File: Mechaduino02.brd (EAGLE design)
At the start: 41.9 x 41.9 mm, 64 parts, among them IC1 SAMD21G18A-AUT, Q1 BSS138, Q2 NFET, Q3 BSS138, Q4 BSS138, Q5 BSS138, U1 TLV70233PDBVR, Y1 32,768Khz

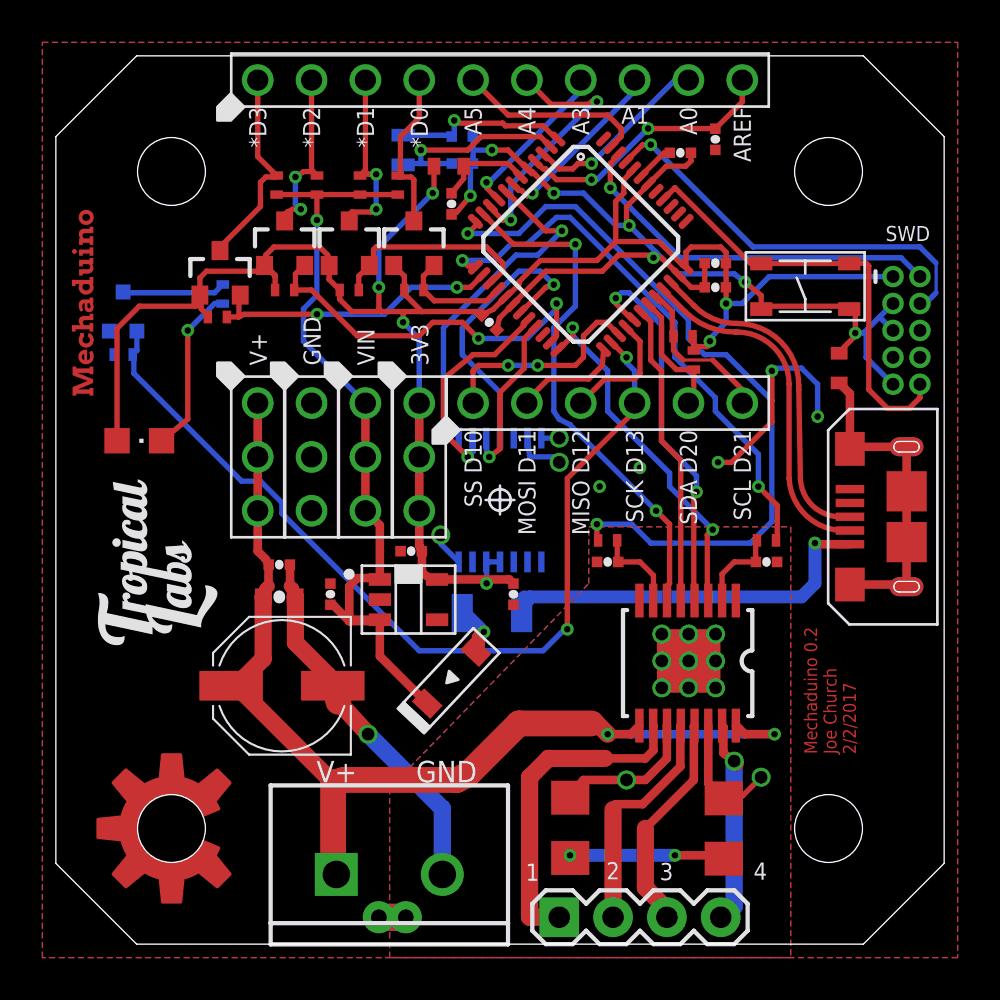
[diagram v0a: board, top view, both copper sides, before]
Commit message: via stitching
cleaned up ground pours
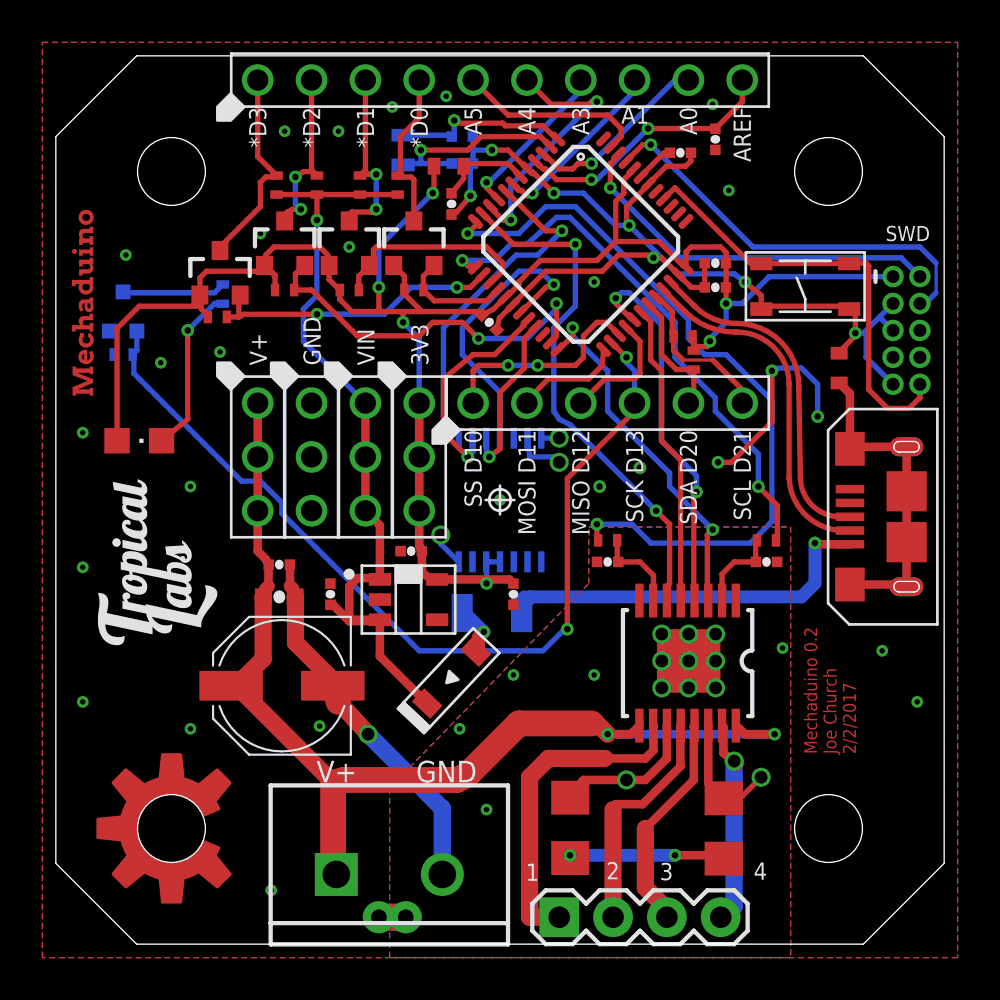
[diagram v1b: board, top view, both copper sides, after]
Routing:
- net GND2: vias 12 -> 17
- net GND: vias 12 -> 34
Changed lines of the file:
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@@
 <wire x1="0" y1="38.1" x2="3.81" y2="41.91" width="0" layer="20"/>
 <wire x1="0" y1="3.81" x2="0" y2="38.1" width="0" layer="20"/>
+<polygon width="0.4064" layer="41">
+<vertex x="-2.159" y="35.306"/>
+<vertex x="1.778" y="35.306"/>
+<vertex x="1.778" y="34.544"/>
+<vertex x="1.651" y="34.544"/>
+<vertex x="1.651" y="25.908"/>
+<vertex x="-1.651" y="25.908"/>
+<vertex x="-1.524" y="25.527"/>
+<vertex x="-2.159" y="25.527"/>
+</polygon>
+<polygon width="0.4064" layer="41">
+<vertex x="37.211" y="33.782"/>
+<vertex x="34.925" y="33.782"/>
+<vertex x="34.925" y="32.893"/>
+<vertex x="38.735" y="32.893"/>
+<vertex x="38.735" y="32.639"/>
+<vertex x="40.386" y="32.639"/>
+<vertex x="40.132" y="32.639"/>
+<vertex x="40.132" y="34.036"/>
+<vertex x="37.211" y="34.036"/>
+</polygon>
+<wire x1="10.541" y1="15.748" x2="10.541" y2="13.208" width="0.4064" layer="41"/>
+<wire x1="10.541" y1="13.208" x2="11.049" y2="13.208" width="0.4064" layer="41"/>
 </plain>
 <attributes>
@@
 <via x="27.559" y="22.479" extent="1-16" drill="0.3048"/>
 <via x="25.654" y="21.59" extent="1-16" drill="0.3048"/>
+<via x="10.795" y="38.354" extent="1-16" drill="0.254" diameter="0.254"/>
+<via x="13.335" y="38.354" extent="1-16" drill="0.254" diameter="0.254"/>
+<via x="13.843" y="32.893" extent="1-16" drill="0.254" diameter="0.254"/>
+<via x="15.875" y="39.497" extent="1-16" drill="0.254" diameter="0.254"/>
+<via x="3.302" y="32.512" extent="1-16" drill="0.254" diameter="0.254"/>
+<via x="20.955" y="20.955" extent="1-16" drill="0.254" diameter="0.254"/>
+<via x="6.35" y="21.59" extent="1-16" drill="0.254" diameter="0.254"/>
+<via x="1.27" y="24.13" extent="1-16" drill="0.254" diameter="0.254"/>
+<via x="1.27" y="11.43" extent="1-16" drill="0.254" diameter="0.254"/>
+<via x="6.35" y="10.16" extent="1-16" drill="0.254" diameter="0.254"/>
+<via x="40.64" y="11.43" extent="1-16" drill="0.254" diameter="0.254"/>
+<via x="10.16" y="2.54" extent="1-16" drill="0.254" diameter="0.254"/>
+<via x="1.27" y="17.78" extent="1-16" drill="0.254" diameter="0.254"/>
+<via x="31.75" y="35.56" extent="1-16" drill="0.254" diameter="0.254"/>
+<via x="9.652" y="33.528" extent="1-16" drill="0.254" diameter="0.254"/>
+<via x="25.4" y="31.242" extent="1-16" drill="0.254" diameter="0.254"/>
+<via x="4.953" y="27.432" extent="1-16" drill="0.254" diameter="0.254"/>
+<via x="7.747" y="27.94" extent="1-16" drill="0.254" diameter="0.254"/>
+<via x="38.989" y="13.843" extent="1-16" drill="0.254" diameter="0.254"/>
+<via x="12.446" y="10.287" extent="1-16" drill="0.254" diameter="0.254"/>
+<via x="30.988" y="39.624" extent="1-16" drill="0.254" diameter="0.254"/>
+<via x="18.415" y="40.005" extent="1-16" drill="0.254" diameter="0.254"/>
 </signal>
 <signal name="RESET">
@@
 <wire x1="11.049" y1="17.907" x2="11.041" y2="17.907" width="0.4064" layer="1"/>
 <wire x1="11.176" y1="16.764" x2="11.291" y2="16.383" width="0.6096" layer="1"/>
+<via x="19.05" y="10.16" extent="1-16" drill="0.254" diameter="0.254"/>
+<via x="25.4" y="12.7" extent="1-16" drill="0.254" diameter="0.254"/>
+<via x="34.29" y="13.97" extent="1-16" drill="0.254" diameter="0.254"/>
+<via x="21.59" y="12.7" extent="1-16" drill="0.254" diameter="0.254"/>
+<via x="20.32" y="6.35" extent="1-16" drill="0.254" diameter="0.254"/>
 </signal>
 <signal name="N$33">

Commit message: fixed xtal caps and power caps to 0603
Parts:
- C6, C7, C8: device swift:0402-CAP -> swift:0603-CAP
- moved C8 0.52 mm to (18.7, 36.7)
- moved C7 0.40 mm to (18.8, 38.2)
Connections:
- removed net N$7: J1.4
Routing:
- net PA01_XOUT32: track 9.52 -> 8.78 mm
- net PA00_XIN32: track 8.54 -> 9.18 mm

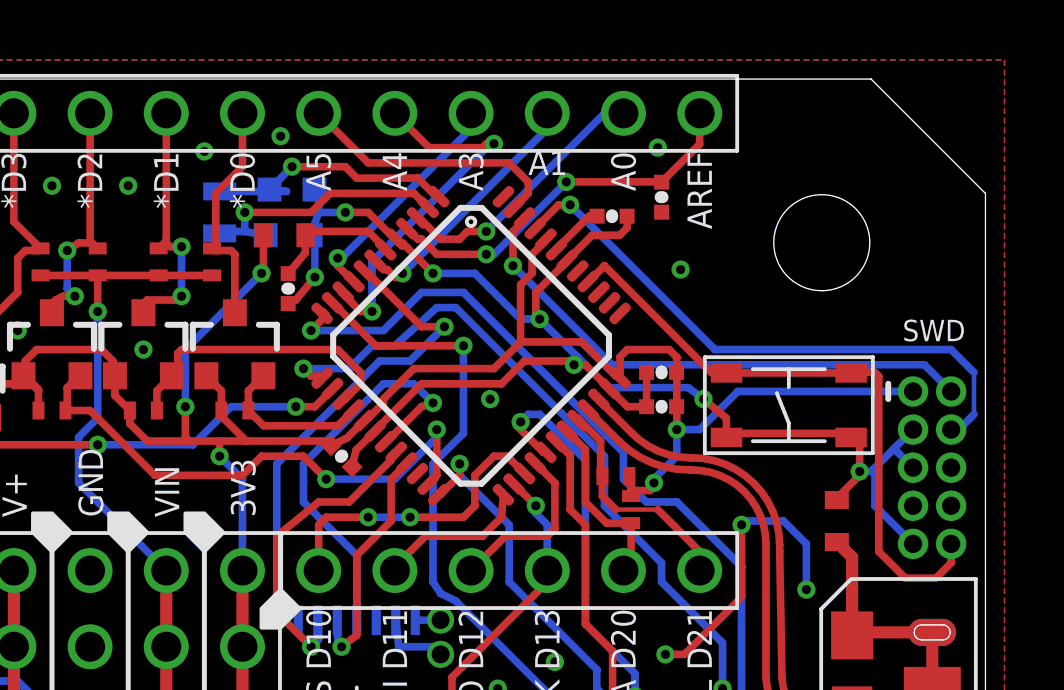
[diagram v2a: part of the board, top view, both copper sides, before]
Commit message: moved vias away from header
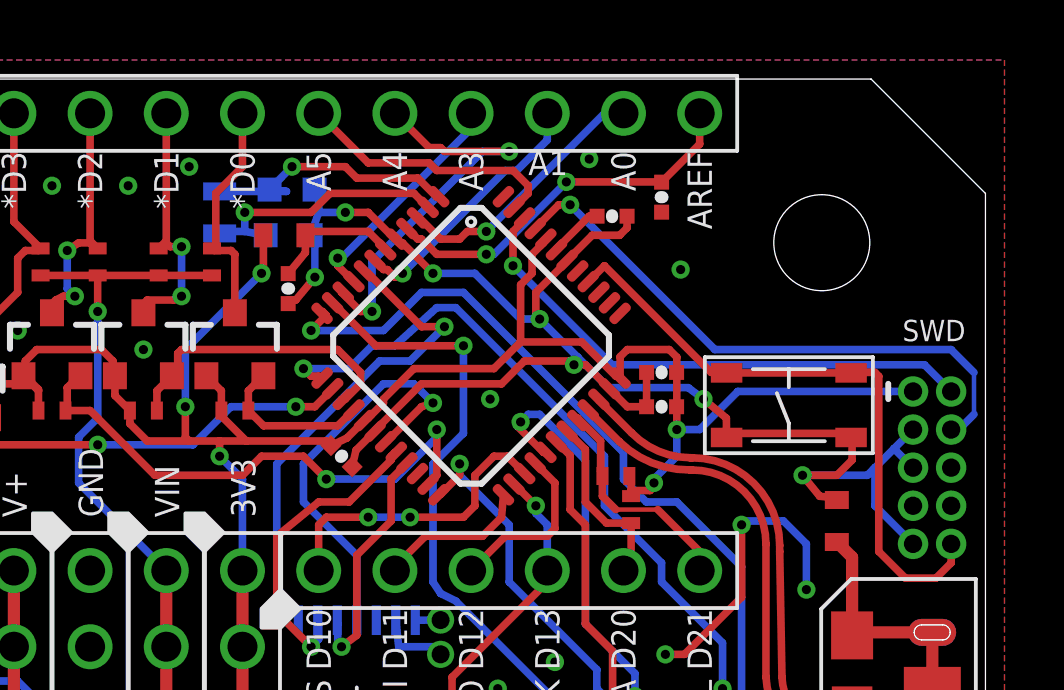
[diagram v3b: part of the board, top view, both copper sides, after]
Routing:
- net GND: track 64.0 -> 67.9 mm, vias 34 -> 33
- net ARDUINO_A4: track 12.5 -> 13.4 mm
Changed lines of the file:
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@@
 <wire x1="37.338" y1="30.099" x2="37.4318" y2="29.9638" width="0.254" layer="1"/>
 <wire x1="33.401" y1="30.099" x2="33.2818" y2="29.9638" width="0.254" layer="1"/>
-<wire x1="37.7825" y1="28.7655" x2="36.957" y2="27.94" width="0.254" layer="1"/>
-<wire x1="37.719" y1="30.099" x2="37.719" y2="28.829" width="0.254" layer="1"/>
+<wire x1="36.3855" y1="28.0035" x2="36.957" y2="27.94" width="0.254" layer="1"/>
+<wire x1="37.719" y1="30.099" x2="37.592" y2="30.099" width="0.254" layer="1"/>
+<wire x1="37.592" y1="30.099" x2="37.465" y2="29.972" width="0.254" layer="1"/>
+<wire x1="37.465" y1="29.972" x2="37.465" y2="29.21" width="0.254" layer="1"/>
+<wire x1="37.465" y1="29.21" x2="36.957" y2="28.702" width="0.254" layer="1"/>
+<wire x1="36.957" y1="28.702" x2="35.814" y2="28.702" width="0.254" layer="1"/>
 <wire x1="37.465" y1="30.099" x2="37.719" y2="30.099" width="0.254" layer="1"/>
 <wire x1="36.957" y1="27.94" x2="36.957" y2="27.878" width="0.254" layer="1"/>
 <wire x1="37.465" y1="30.099" x2="37.4318" y2="29.9638" width="0.254" layer="1"/>
-<wire x1="38.1" y1="28.829" x2="37.719" y2="28.829" width="0.254" layer="16"/>
+<wire x1="38.1635" y1="28.8925" x2="37.973" y2="28.702" width="0.254" layer="16"/>
+<wire x1="37.973" y1="28.702" x2="35.814" y2="28.702" width="0.254" layer="16"/>
 <wire x1="39.497" y1="30.226" x2="38.862" y2="29.591" width="0.254" layer="16"/>
-<wire x1="38.862" y1="29.591" x2="38.1635" y2="28.8925" width="0.254" layer="16"/>
-<wire x1="38.1635" y1="28.8925" x2="38.1" y2="28.829" width="0.254" layer="16"/>
-<wire x1="37.719" y1="28.829" x2="37.7825" y2="28.7655" width="0.254" layer="1"/>
-<via x="37.719" y="28.829" extent="1-16" drill="0.3048" diameter="0.254"/>
+<wire x1="38.862" y1="29.591" x2="38.227" y2="28.956" width="0.254" layer="16"/>
+<wire x1="35.814" y1="28.702" x2="36.3855" y2="28.0035" width="0.254" layer="1"/>
+<via x="35.814" y="28.702" extent="1-16" drill="0.3048" diameter="0.254"/>
 <wire x1="38.862" y1="29.591" x2="39.497" y2="28.956" width="0.254" layer="16"/>
 <wire x1="38.227" y1="27.686" x2="39.497" y2="26.416" width="0.254" layer="16"/>
-<wire x1="38.227" y1="28.829" x2="38.227" y2="27.686" width="0.254" layer="16"/>
-<wire x1="38.227" y1="28.829" x2="38.1635" y2="28.8925" width="0.254" layer="16"/>
+<wire x1="38.227" y1="28.956" x2="38.227" y2="27.686" width="0.254" layer="16"/>
+<wire x1="38.227" y1="28.956" x2="38.1635" y2="28.8925" width="0.254" layer="16"/>
 <wire x1="32.512" y1="31.242" x2="33.274" y2="30.607" width="0.254" layer="1"/>
 <wire x1="32.004" y1="31.623" x2="32.512" y2="31.242" width="0.254" layer="16"/>
@@
 <via x="13.335" y="38.354" extent="1-16" drill="0.3048" diameter="0.254"/>
 <via x="13.843" y="32.893" extent="1-16" drill="0.3048" diameter="0.254"/>
-<via x="15.875" y="39.497" extent="1-16" drill="0.3048" diameter="0.254"/>
+<via x="15.367" y="38.989" extent="1-16" drill="0.3048" diameter="0.254"/>
 <via x="3.302" y="32.512" extent="1-16" drill="0.3048" diameter="0.254"/>
 <via x="20.955" y="20.955" extent="1-16" drill="0.3048" diameter="0.254"/>
@@
 <via x="38.989" y="13.843" extent="1-16" drill="0.3048" diameter="0.254"/>
 <via x="12.446" y="10.287" extent="1-16" drill="0.3048" diameter="0.254"/>
-<via x="30.988" y="39.624" extent="1-16" drill="0.3048" diameter="0.254"/>
-<via x="18.415" y="40.005" extent="1-16" drill="0.3048" diameter="0.254"/>
+<via x="28.702" y="39.243" extent="1-16" drill="0.3048" diameter="0.254"/>
 </signal>
 <signal name="RESET">
@@
 <contactref element="IC1" pad="7"/>
 <contactref element="J2" pad="P$8"/>
-<wire x1="27.305" y1="40.259" x2="27.305" y2="40.767" width="0.254" layer="16"/>
-<wire x1="22.479" y1="35.433" x2="27.305" y2="40.259" width="0.254" layer="16"/>
+<wire x1="27.305" y1="39.878" x2="27.305" y2="40.767" width="0.254" layer="16"/>
+<wire x1="22.479" y1="35.433" x2="25.908" y2="38.862" width="0.254" layer="16"/>
+<wire x1="25.908" y1="38.862" x2="26.289" y2="38.862" width="0.254" layer="16"/>
+<wire x1="26.289" y1="38.862" x2="27.305" y2="39.878" width="0.254" layer="16"/>
 <wire x1="22.352" y1="35.433" x2="22.479" y2="35.433" width="0.254" layer="1"/>
 <wire x1="22.225" y1="35.306" x2="22.352" y2="35.433" width="0.254" layer="1"/>
@@
 <contactref element="IC1" pad="10"/>
 <contactref element="J2" pad="P$6"/>
-<wire x1="25.4" y1="39.751" x2="21.463" y2="35.814" width="0.254" layer="16"/>
-<wire x1="25.527" y1="39.751" x2="25.4" y2="39.751" width="0.254" layer="16"/>
-<wire x1="25.273" y1="39.751" x2="25.527" y2="39.751" width="0.254" layer="1"/>
-<wire x1="25.146" y1="39.624" x2="25.273" y2="39.751" width="0.254" layer="1"/>
-<wire x1="23.368" y1="39.624" x2="25.146" y2="39.624" width="0.254" layer="1"/>
+<wire x1="25.146" y1="39.497" x2="21.463" y2="35.814" width="0.254" layer="16"/>
+<wire x1="26.035" y1="39.497" x2="25.146" y2="39.497" width="0.254" layer="16"/>
+<wire x1="23.368" y1="39.624" x2="23.749" y2="39.624" width="0.254" layer="1"/>
+<wire x1="23.749" y1="39.624" x2="23.876" y2="39.497" width="0.254" layer="1"/>
+<wire x1="23.876" y1="39.497" x2="26.035" y2="39.497" width="0.254" layer="1"/>
 <wire x1="22.225" y1="40.767" x2="23.368" y2="39.624" width="0.254" layer="1"/>
 <wire x1="21.463" y1="34.163" x2="21.463" y2="35.814" width="0.254" layer="16"/>
@@
 <wire x1="21.082" y1="34.163" x2="21.463" y2="34.163" width="0.254" layer="1"/>
 <wire x1="20.447" y1="34.798" x2="20.50468125" y2="34.80544375" width="0.254" layer="1"/>
-<via x="25.527" y="39.751" extent="1-16" drill="0.3048" diameter="0.254"/>
+<via x="26.035" y="39.497" extent="1-16" drill="0.3048" diameter="0.254"/>
 <via x="21.463" y="34.163" extent="1-16" drill="0.3048" diameter="0.254"/>
 </signal>
@@
 <contactref element="J2" pad="P$5"/>
 <wire x1="19.685" y1="40.767" x2="21.336" y2="39.116" width="0.254" layer="1"/>
-<wire x1="21.336" y1="39.116" x2="26.035" y2="39.116" width="0.254" layer="1"/>
-<wire x1="26.035" y1="39.116" x2="26.67" y2="38.481" width="0.254" layer="1"/>
-<wire x1="26.67" y1="38.481" x2="26.67" y2="38.1" width="0.254" layer="1"/>
+<wire x1="21.336" y1="39.116" x2="23.368" y2="39.116" width="0.254" layer="1"/>
+<wire x1="23.368" y1="39.116" x2="23.622" y2="38.862" width="0.254" layer="1"/>
+<wire x1="23.622" y1="38.862" x2="26.162" y2="38.862" width="0.254" layer="1"/>
+<wire x1="26.162" y1="38.862" x2="26.67" y2="38.354" width="0.254" layer="1"/>
+<wire x1="26.67" y1="38.354" x2="26.67" y2="38.1" width="0.254" layer="1"/>
 <wire x1="26.67" y1="38.1" x2="26.20386875" y2="37.63386875" width="0.254" layer="1"/>
 <wire x1="26.20386875" y1="37.63386875" x2="26.196890625" y2="37.63386875" width="0.254" layer="1"/>
@@
 </signal>
 </signals>
+<errors>
+</errors>
 </board>
 </drawing>
